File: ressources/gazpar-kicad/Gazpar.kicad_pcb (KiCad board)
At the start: 2 copper layers, 44.4 x 24.8 mm, 9 parts, among them J1 Alim, U1 PC817, U2 ESP-01S, U3 AMS1117

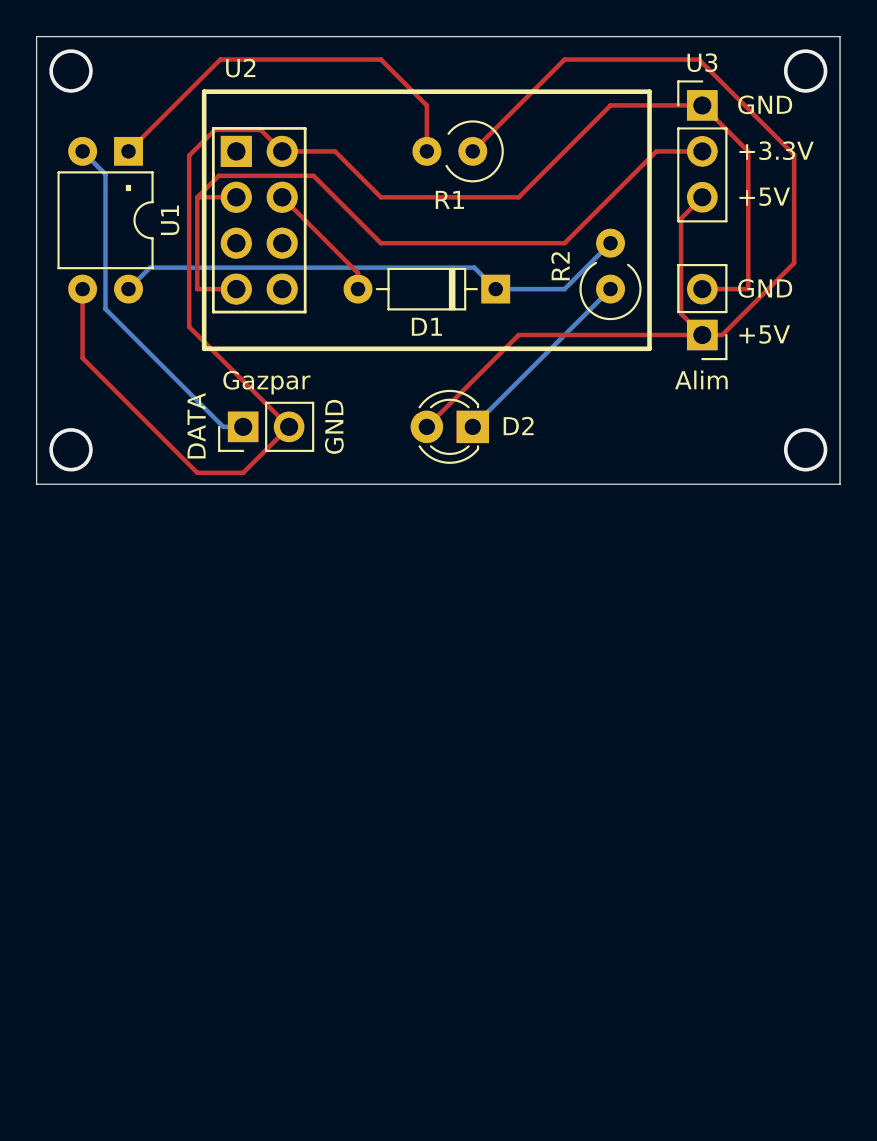
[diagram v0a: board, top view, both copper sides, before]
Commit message: doc(gazpar): move from esp01 to esp32
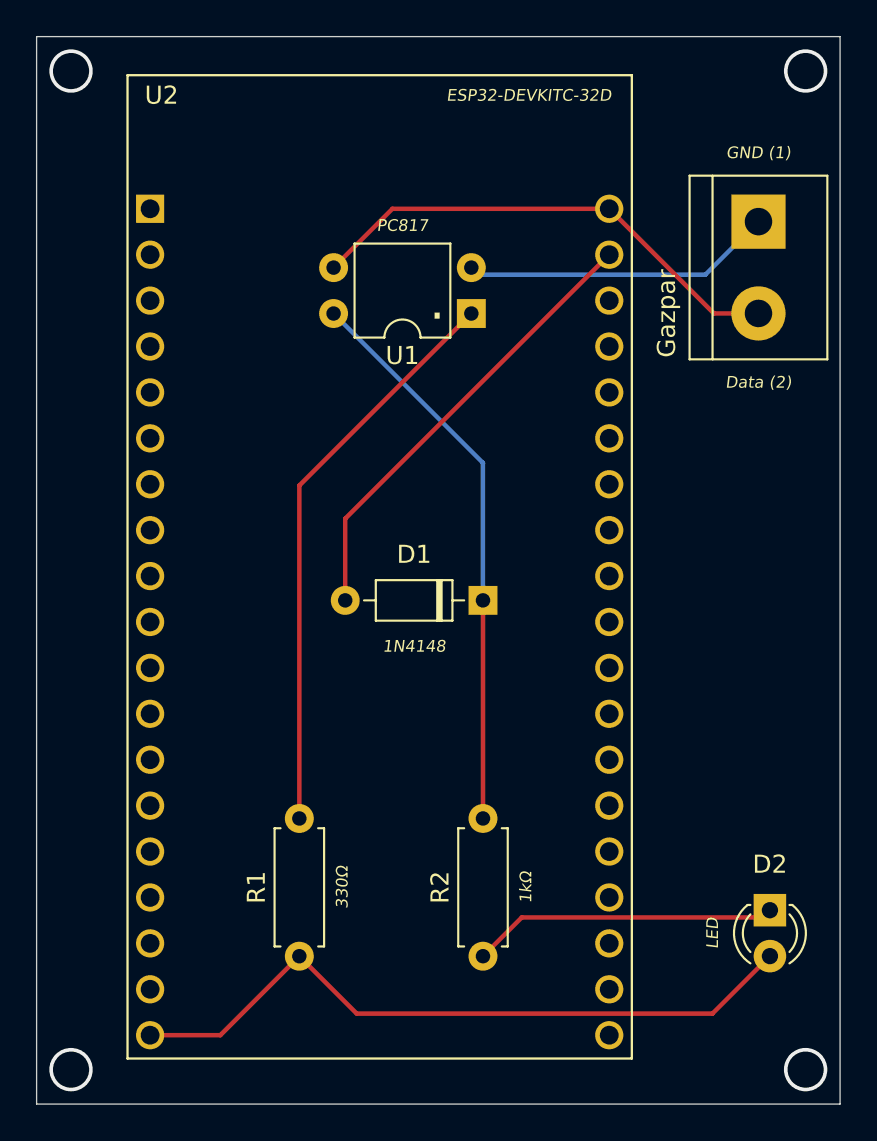
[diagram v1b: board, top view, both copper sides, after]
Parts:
- removed the Gazpar at (157.5, 61.0)
- removed J1: Alim, Connector_PinHeader_2.54mm:PinHeader_1x02_P2.54mm_Vertical
- removed U3: AMS1117, Connector_PinHeader_2.54mm:PinHeader_1x03_P2.54mm_Vertical
- added Gazpar: G-, TerminalBlock:TerminalBlock_bornier-2_P5.08mm, F.Cu at (186.0, 49.6)
- R1: value 330 -> 330Ω; footprint Resistor_THT:R_Axial_DIN0309_L9.0mm_D3.2mm_P2.54mm_Vertical -> Resistor_THT:R_Axial_DIN0207_L6.3mm_D2.5mm_P7.62mm_Horizontal
- R2: value 1k -> 1kΩ; footprint Resistor_THT:R_Axial_DIN0309_L9.0mm_D3.2mm_P2.54mm_Vertical -> Resistor_THT:R_Axial_DIN0207_L6.3mm_D2.5mm_P7.62mm_Horizontal
- U2: value ESP-01S -> ESP32-DEVKITC-32D; footprint ESP8266:ESP-01 -> ESP32-DEVKITC-32D:MODULE_ESP32-DEVKITC-32D
- moved R1 45.5 mm to (160.6, 90.2), turned to 90 degrees
- moved R2 37.6 mm to (170.7, 90.2)
- moved D2 31.4 mm to (186.6, 87.7), turned to -90 degrees
- moved U2 24.3 mm to (165.0, 68.7)
- moved U1 21.0 mm to (170.1, 54.7), turned to 180 degrees
- moved D1 17.2 mm to (170.7, 70.6)
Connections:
- D2 pad 2: +5V -> Net-(D2-Pad2)
- R1 pad 1: +5V -> Net-(D2-Pad2)
- U1 pad 3: GND -> Net-(Gazpar1-Pad2)
- U2 pad 2: GND -> unconnected-(U2-Pad2)
- U2 pad 3: Net-(U2-Pad3) -> unconnected-(U2-Pad3)
- U2 pad 4: Net-(D1-Pad2) -> unconnected-(U2-Pad4)
- U2 pad 7: Net-(U2-Pad3) -> unconnected-(U2-Pad7)
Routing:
- net GND: track 82.6 -> 0.00 mm
- net +5V: track 60.7 -> 0.00 mm
- net Net-(U2-Pad3): track 41.5 -> 0.00 mm
- net Net-(D2-Pad2): track 0.00 -> 38.7 mm
- net Net-(Gazpar1-Pad2): track 0.00 -> 27.3 mm
- net Net-(D1-Pad2): track 6.82 -> 25.2 mm
- net Net-(R1-Pad2): track 22.2 -> 31.9 mm
- net Net-(D2-Pad1): track 10.8 -> 16.9 mm
- net Net-(D1-Pad1): track 28.7 -> 31.4 mm
- net Net-(Gazpar1-Pad1): track 19.6 -> 17.3 mm
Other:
- board size 44.4 x 24.8 mm -> 44.4 x 59.1 mm
- board text added: "Data (2)"
- board text added: "GND (1)"
- board text removed: "+3.3V"
- board text removed: "+5V"
- board text removed: "DATA"
- board text removed: "GND"
